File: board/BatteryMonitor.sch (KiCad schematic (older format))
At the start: 20 parts, among them J1 Screw_Terminal_01x02, J2 Screw_Terminal_01x02, Q1 IPP80P03P4L-04, Q2 2N7000, Q3 IPP80P03P4L-04, U1 OKI-78SR-5_1.5-W36H-C, U2 INA260

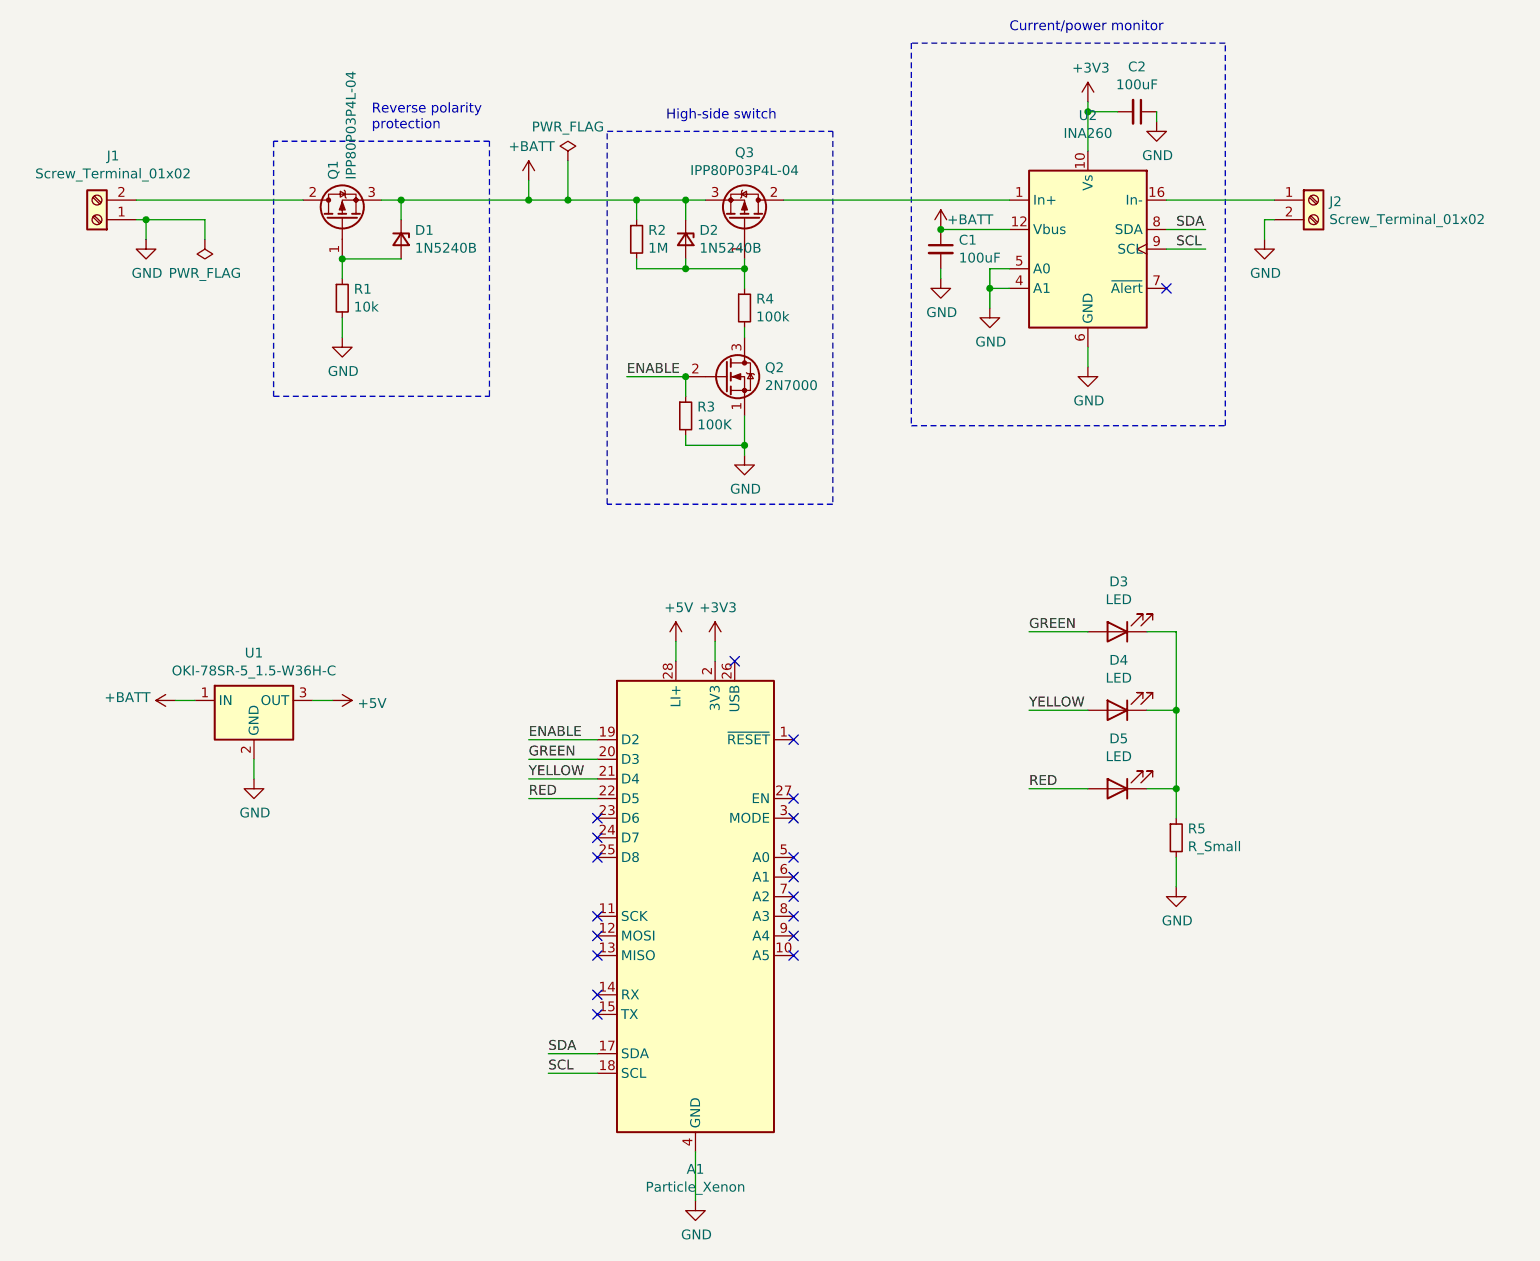
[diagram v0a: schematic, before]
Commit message: Assign footprints and begin board layout
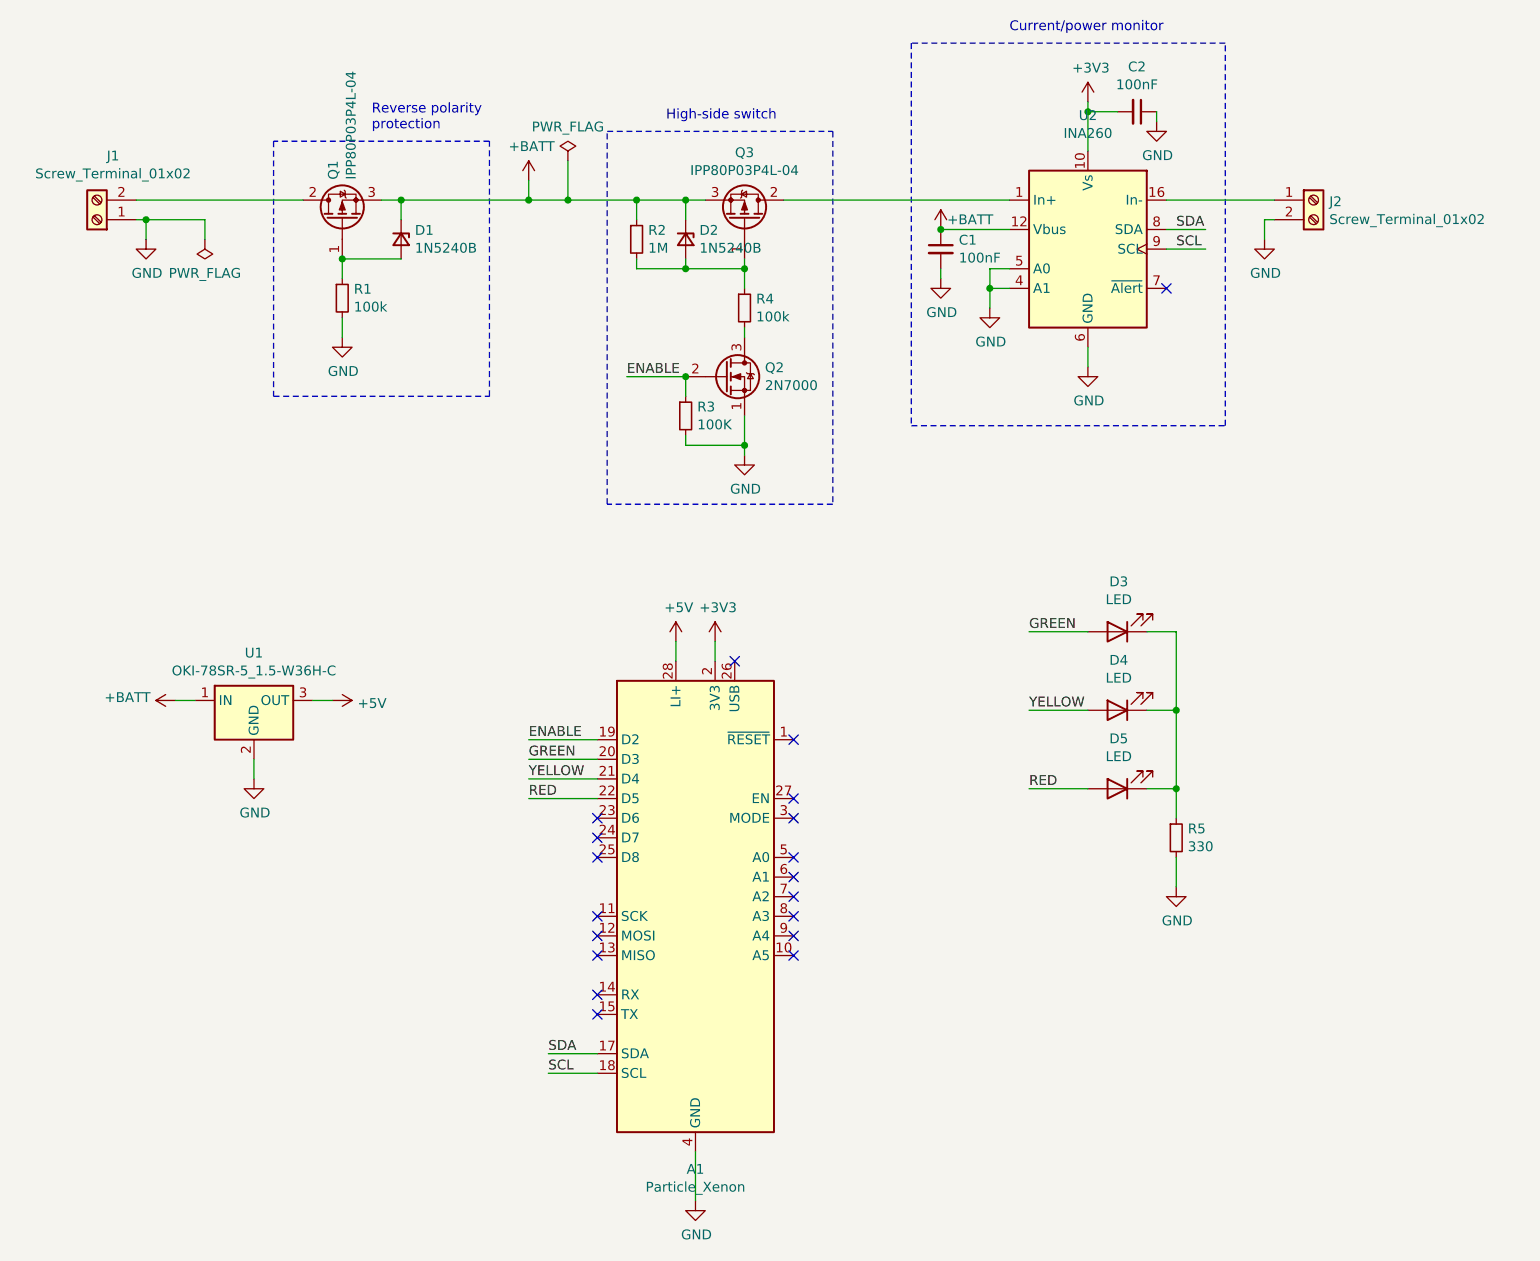
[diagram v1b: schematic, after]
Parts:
- A1: footprint Module:Adafruit_Feather -> SaintGimp:Adafruit_Feather
- C1, C2: value 100uF -> 100nF; footprint (none) -> Capacitor_SMD:C_0805_2012Metric_Pad1.15x1.40mm_HandSolder
- D3, D4, D5: footprint (none) -> LED_THT:LED_D3.0mm
- J1, J2: footprint (none) -> TerminalBlock_Phoenix:TerminalBlock_Phoenix_MKDS-1,5-2-5.08_1x02_P5.08mm_Horizontal
- R1: value 10k -> 100k; footprint (none) -> Resistor_SMD:R_0805_2012Metric_Pad1.15x1.40mm_HandSolder
- R2, R3, R4: footprint (none) -> Resistor_SMD:R_0805_2012Metric_Pad1.15x1.40mm_HandSolder
- R5: value R_Small -> 330; footprint (none) -> Resistor_SMD:R_0805_2012Metric_Pad1.15x1.40mm_HandSolder
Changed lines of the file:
@@
 F 0 "A1" H 4450 3911 50  0000 C CNN
 F 1 "Particle_Xenon" H 4450 3820 50  0000 C CNN
-F 2 "Module:Adafruit_Feather" H 4550 3950 50  0001 L CNN
+F 2 "SaintGimp:Adafruit_Feather" H 4550 3950 50  0001 L CNN
 F 3 "https://docs.particle.io/datasheets/discontinued/xenon-datasheet/" H 4450 4500 50  0001 C CNN
 	1    4450 5300
@@
 F 0 "J1" H 1318 1525 50  0000 C CNN
 F 1 "Screw_Terminal_01x02" H 1318 1616 50  0000 C CNN
-F 2 "" H 1400 1850 50  0001 C CNN
+F 2 "TerminalBlock_Phoenix:TerminalBlock_Phoenix_MKDS-1,5-2-5.08_1x02_P5.08mm_Horizontal" H 1400 1850 50  0001 C CNN
 F 3 "~" H 1400 1850 50  0001 C CNN
 	1    1400 1850
@@
 P 2650 2250
 F 0 "R1" H 2709 2296 50  0000 L CNN
-F 1 "10k" H 2709 2205 50  0000 L CNN
-F 2 "" H 2650 2250 50  0001 C CNN
+F 1 "100k" H 2709 2205 50  0000 L CNN
+F 2 "Resistor_SMD:R_0805_2012Metric_Pad1.15x1.40mm_HandSolder" H 2650 2250 50  0001 C CNN
 F 3 "~" H 2650 2250 50  0001 C CNN
 	1    2650 2250
@@
 F 0 "R4" H 4759 2346 50  0000 L CNN
 F 1 "100k" H 4759 2255 50  0000 L CNN
-F 2 "" H 4700 2300 50  0001 C CNN
+F 2 "Resistor_SMD:R_0805_2012Metric_Pad1.15x1.40mm_HandSolder" H 4700 2300 50  0001 C CNN
 F 3 "~" H 4700 2300 50  0001 C CNN
 	1    4700 2300
@@
 F 0 "J2" H 7680 1742 50  0000 L CNN
 F 1 "Screw_Terminal_01x02" H 7680 1651 50  0000 L CNN
-F 2 "" H 7600 1750 50  0001 C CNN
+F 2 "TerminalBlock_Phoenix:TerminalBlock_Phoenix_MKDS-1,5-2-5.08_1x02_P5.08mm_Horizontal" H 7600 1750 50  0001 C CNN
 F 3 "~" H 7600 1750 50  0001 C CNN
 	1    7600 1750
@@
 F 0 "D3" H 6593 3695 50  0000 C CNN
 F 1 "LED" H 6593 3786 50  0000 C CNN
-F 2 "" H 6600 3950 50  0001 C CNN
+F 2 "LED_THT:LED_D3.0mm" H 6600 3950 50  0001 C CNN
 F 3 "~" H 6600 3950 50  0001 C CNN
 	1    6600 3950
@@
 F 0 "D4" H 6593 4095 50  0000 C CNN
 F 1 "LED" H 6593 4186 50  0000 C CNN
-F 2 "" H 6600 4350 50  0001 C CNN
+F 2 "LED_THT:LED_D3.0mm" H 6600 4350 50  0001 C CNN
 F 3 "~" H 6600 4350 50  0001 C CNN
 	1    6600 4350
@@
 F 0 "D5" H 6593 4495 50  0000 C CNN
 F 1 "LED" H 6593 4586 50  0000 C CNN
-F 2 "" H 6600 4750 50  0001 C CNN
+F 2 "LED_THT:LED_D3.0mm" H 6600 4750 50  0001 C CNN
 F 3 "~" H 6600 4750 50  0001 C CNN
 	1    6600 4750
@@
 P 6900 5000
 F 0 "R5" H 6959 5046 50  0000 L CNN
-F 1 "R_Small" H 6959 4955 50  0000 L CNN
-F 2 "" H 6900 5000 50  0001 C CNN
+F 1 "330" H 6959 4955 50  0000 L CNN
+F 2 "Resistor_SMD:R_0805_2012Metric_Pad1.15x1.40mm_HandSolder" H 6900 5000 50  0001 C CNN
 F 3 "~" H 6900 5000 50  0001 C CNN
 	1    6900 5000
@@
 F 0 "R3" H 4459 2896 50  0000 L CNN
 F 1 "100K" H 4459 2805 50  0000 L CNN
-F 2 "" H 4400 2850 50  0001 C CNN
+F 2 "Resistor_SMD:R_0805_2012Metric_Pad1.15x1.40mm_HandSolder" H 4400 2850 50  0001 C CNN
 F 3 "~" H 4400 2850 50  0001 C CNN
 	1    4400 2850
@@
 F 0 "R2" H 4209 1996 50  0000 L CNN
 F 1 "1M" H 4209 1905 50  0000 L CNN
-F 2 "" H 4150 1950 50  0001 C CNN
+F 2 "Resistor_SMD:R_0805_2012Metric_Pad1.15x1.40mm_HandSolder" H 4150 1950 50  0001 C CNN
 F 3 "~" H 4150 1950 50  0001 C CNN
 	1    4150 1950
@@
 P 6700 1300
 F 0 "C2" V 6471 1300 50  0000 C CNN
-F 1 "100uF" V 6562 1300 50  0000 C CNN
-F 2 "" H 6700 1300 50  0001 C CNN
+F 1 "100nF" V 6562 1300 50  0000 C CNN
+F 2 "Capacitor_SMD:C_0805_2012Metric_Pad1.15x1.40mm_HandSolder" H 6700 1300 50  0001 C CNN
 F 3 "~" H 6700 1300 50  0001 C CNN
 	1    6700 1300
@@
 P 5700 2000
 F 0 "C1" H 5792 2046 50  0000 L CNN
-F 1 "100uF" H 5792 1955 50  0000 L CNN
-F 2 "" H 5700 2000 50  0001 C CNN
+F 1 "100nF" H 5792 1955 50  0000 L CNN
+F 2 "Capacitor_SMD:C_0805_2012Metric_Pad1.15x1.40mm_HandSolder" H 5700 2000 50  0001 C CNN
 F 3 "~" H 5700 2000 50  0001 C CNN
 	1    5700 2000

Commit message: Finish layout, first spin
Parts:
- added R6, R7: 330, Resistor_SMD:R_0805_2012Metric_Pad1.15x1.40mm_HandSolder, symbol Device:R_Small
- Q1, Q3: footprint Package_TO_SOT_THT:TO-220-3_Vertical -> Package_TO_SOT_THT:TO-220-3_Horizontal_TabDown
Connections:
- net GND: now also R5.1, R6.1, R7.1; no longer R5.2
- new net: D4.1 (K), R6.2
- new net: D5.1 (K), R7.2
- new net: D3.1 (K), R5.2
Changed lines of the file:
@@
 F 0 "Q1" H 2854 1896 50  0000 L CNN
 F 1 "IPP80P03P4L-04" H 2854 1805 50  0000 L CNN
-F 2 "Package_TO_SOT_THT:TO-220-3_Vertical" H 2850 1775 50  0001 L CIN
+F 2 "Package_TO_SOT_THT:TO-220-3_Horizontal_TabDown" H 2850 1775 50  0001 L CIN
 F 3 "https://www.infineon.com/dgdl/Infineon-I80P03P4L_04-DS-v01_01-en.pdf?fileId=db3a30431ddc9372011e07e95eb827d7" H 2650 1850 50  0001 L CNN
 	1    2650 1850
@@
 F 0 "Q3" V 5042 1850 50  0000 C CNN
 F 1 "IPP80P03P4L-04" V 4951 1850 50  0000 C CNN
-F 2 "Package_TO_SOT_THT:TO-220-3_Vertical" H 4900 1775 50  0001 L CIN
+F 2 "Package_TO_SOT_THT:TO-220-3_Horizontal_TabDown" H 4900 1775 50  0001 L CIN
 F 3 "https://www.infineon.com/dgdl/Infineon-I80P03P4L_04-DS-v01_01-en.pdf?fileId=db3a30431ddc9372011e07e95eb827d7" H 4700 1850 50  0001 L CNN
 	1    4700 1850
@@
 $EndComp
 $Comp
-L Device:R_Small R5
-U 1 1 5F81F916
-P 6900 5000
-F 0 "R5" H 6959 5046 50  0000 L CNN
-F 1 "330" H 6959 4955 50  0000 L CNN
-F 2 "Resistor_SMD:R_0805_2012Metric_Pad1.15x1.40mm_HandSolder" H 6900 5000 50  0001 C CNN
-F 3 "~" H 6900 5000 50  0001 C CNN
-	1    6900 5000
-	1    0    0    -1
-$EndComp
-$Comp
 L power:GND #PWR014
 U 1 1 5F820E28
-P 6900 5250
-F 0 "#PWR014" H 6900 5000 50  0001 C CNN
-F 1 "GND" H 6905 5077 50  0000 C CNN
-F 2 "" H 6900 5250 50  0001 C CNN
-F 3 "" H 6900 5250 50  0001 C CNN
-	1    6900 5250
-	1    0    0    -1
-$EndComp
-Wire Wire Line
-	6900 5250 6900 5100
-Wire Wire Line
-	6900 4900 6900 4750
+P 7200 4950
+F 0 "#PWR014" H 7200 4700 50  0001 C CNN
+F 1 "GND" H 7205 4777 50  0000 C CNN
+F 2 "" H 7200 4950 50  0001 C CNN
+F 3 "" H 7200 4950 50  0001 C CNN
+	1    7200 4950
+	1    0    0    -1
+$EndComp
 Wire Wire Line
 	6900 3950 6750 3950
 Wire Wire Line
 	6750 4350 6900 4350
-Connection ~ 6900 4350
-Wire Wire Line
-	6900 4350 6900 3950
 Wire Wire Line
 	6750 4750 6900 4750
-Connection ~ 6900 4750
-Wire Wire Line
-	6900 4750 6900 4350
 Wire Wire Line
 	6450 3950 6150 3950
@@
 Wire Wire Line
 	3800 1750 3600 1750
+Wire Wire Line
+	7100 3950 7200 3950
+Wire Wire Line
+	7200 3950 7200 4350
+$Comp
+L Device:R_Small R6
+U 1 1 5F818E57
+P 7000 4350
+F 0 "R6" V 6804 4350 50  0000 C CNN
+F 1 "330" V 6895 4350 50  0000 C CNN
+F 2 "Resistor_SMD:R_0805_2012Metric_Pad1.15x1.40mm_HandSolder" H 7000 4350 50  0001 C CNN
+F 3 "~" H 7000 4350 50  0001 C CNN
+	1    7000 4350
+	0    1    1    0
+$EndComp
+$Comp
+L Device:R_Small R7
+U 1 1 5F81954C
+P 7000 4750
+F 0 "R7" V 6804 4750 50  0000 C CNN
+F 1 "330" V 6895 4750 50  0000 C CNN
+F 2 "Resistor_SMD:R_0805_2012Metric_Pad1.15x1.40mm_HandSolder" H 7000 4750 50  0001 C CNN
+F 3 "~" H 7000 4750 50  0001 C CNN
+	1    7000 4750
+	0    1    1    0
+$EndComp
+Wire Wire Line
+	7100 4350 7200 4350
+Connection ~ 7200 4350
+Wire Wire Line
+	7200 4350 7200 4750
+Wire Wire Line
+	7100 4750 7200 4750
+Connection ~ 7200 4750
+Wire Wire Line
+	7200 4750 7200 4950
+$Comp
+L Device:R_Small R5
+U 1 1 5F822328
+P 7000 3950
+F 0 "R5" V 6804 3950 50  0000 C CNN
+F 1 "330" V 6895 3950 50  0000 C CNN
+F 2 "Resistor_SMD:R_0805_2012Metric_Pad1.15x1.40mm_HandSolder" H 7000 3950 50  0001 C CNN
+F 3 "~" H 7000 3950 50  0001 C CNN
+	1    7000 3950
+	0    1    1    0
+$EndComp
 $EndSCHEMATC
